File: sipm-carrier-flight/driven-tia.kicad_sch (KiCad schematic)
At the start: 10 parts, among them U1 LTC6268xS8-10, U2 BUF602xD

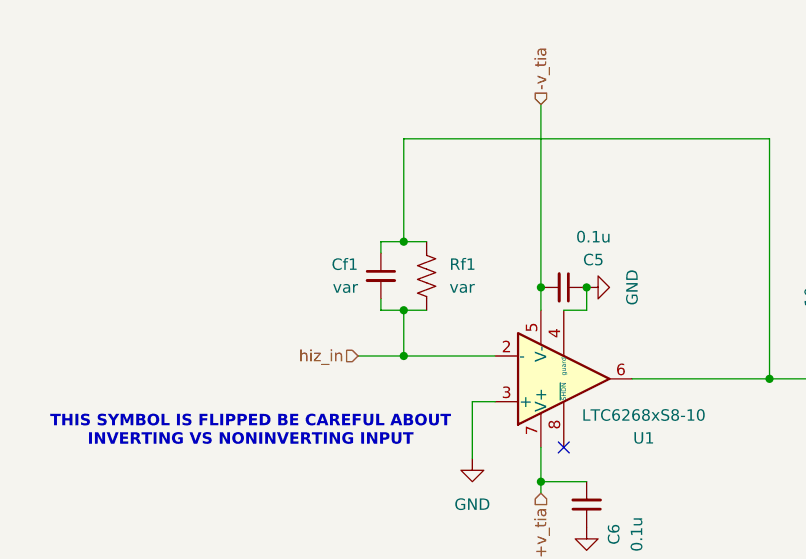
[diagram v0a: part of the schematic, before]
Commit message: sipm board pre-production
- verify spcaing between SiPMs
- move silkscreens around so that they are not overlapping
- change footprints to be hand-solder type in case someone has to do that
- change values of some components to unify part list (e.g. any 100n are now 0.1u)
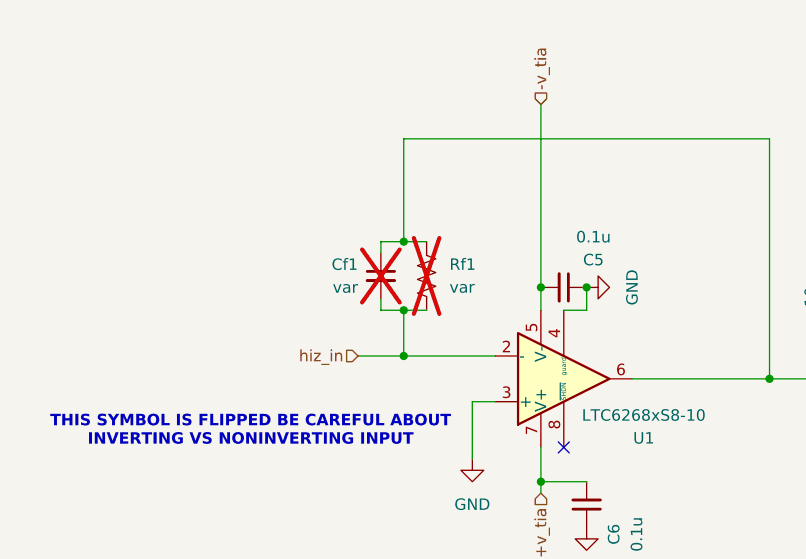
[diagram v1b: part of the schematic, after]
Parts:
- C5, C6, C7, C8: footprint Capacitor_SMD:C_1206_3216Metric -> Capacitor_SMD:C_1206_3216Metric_Pad1.33x1.80mm_HandSolder
- Cf1, Rf1: now not fitted; now left out of the parts list
- Rt2: footprint Resistor_SMD:R_0805_2012Metric -> Resistor_SMD:R_0805_2012Metric_Pad1.20x1.40mm_HandSolder
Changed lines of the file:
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@@
 			)
 		)
-		(property "Footprint" "Capacitor_SMD:C_1206_3216Metric"
+		(property "Footprint" "Capacitor_SMD:C_1206_3216Metric_Pad1.33x1.80mm_HandSolder"
 			(at 138.43 71.12 0)
 			(effects
@@
 			)
 		)
-		(property "Footprint" "Capacitor_SMD:C_1206_3216Metric"
+		(property "Footprint" "Capacitor_SMD:C_1206_3216Metric_Pad1.33x1.80mm_HandSolder"
 			(at 93.98 102.87 0)
 			(effects
@@
 			)
 		)
-		(property "Footprint" "Capacitor_SMD:C_1206_3216Metric"
+		(property "Footprint" "Capacitor_SMD:C_1206_3216Metric_Pad1.33x1.80mm_HandSolder"
 			(at 91.44 78.74 0)
 			(effects
@@
 			)
 		)
-		(property "Footprint" "Resistor_SMD:R_0805_2012Metric"
+		(property "Footprint" "Resistor_SMD:R_0805_2012Metric_Pad1.20x1.40mm_HandSolder"
 			(at 156.464 89.916 90)
 			(effects
@@
 		(unit 1)
 		(exclude_from_sim no)
-		(in_bom yes)
-		(on_board yes)
-		(dnp no)
+		(in_bom no)
+		(on_board yes)
+		(dnp yes)
 		(fields_autoplaced yes)
 		(property "Reference" "Rf1"
@@
 		(unit 1)
 		(exclude_from_sim no)
-		(in_bom yes)
-		(on_board yes)
-		(dnp no)
+		(in_bom no)
+		(on_board yes)
+		(dnp yes)
 		(property "Reference" "Cf1"
 			(at 68.58 76.2062 0)
@@
 			)
 		)
-		(property "Footprint" "Capacitor_SMD:C_1206_3216Metric"
+		(property "Footprint" "Capacitor_SMD:C_1206_3216Metric_Pad1.33x1.80mm_HandSolder"
 			(at 135.89 129.54 0)
 			(effects
